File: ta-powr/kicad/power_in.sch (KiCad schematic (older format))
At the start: 29 parts, among them U1 SPV1040, U3 TLV8544DT, U4 ADS1115-Q1

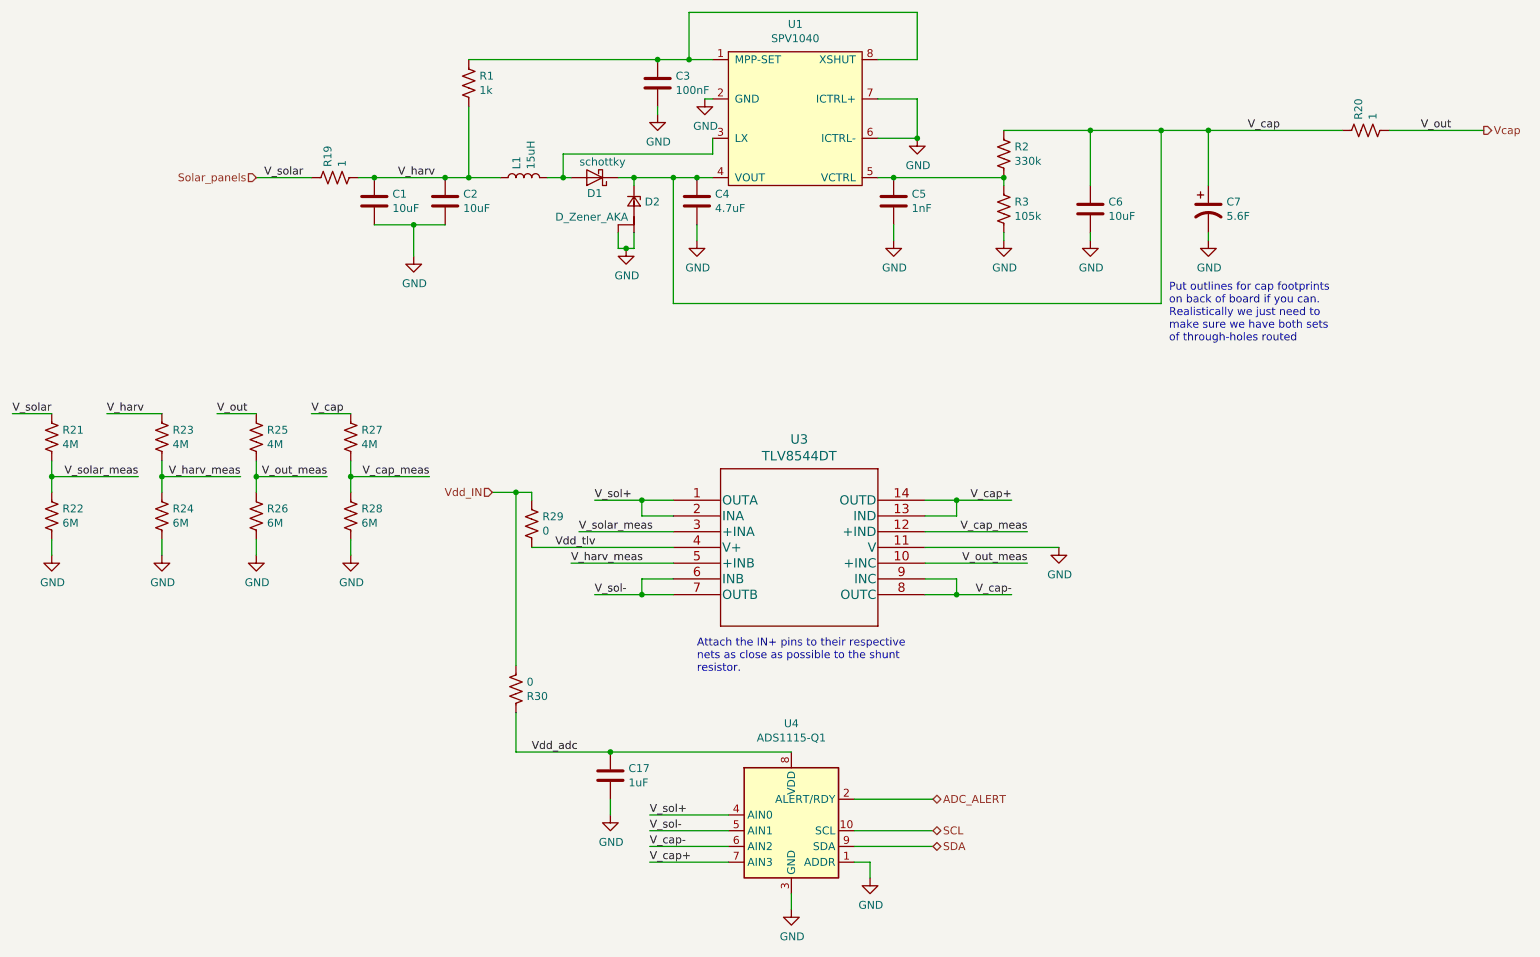
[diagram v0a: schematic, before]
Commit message: updated parts lists
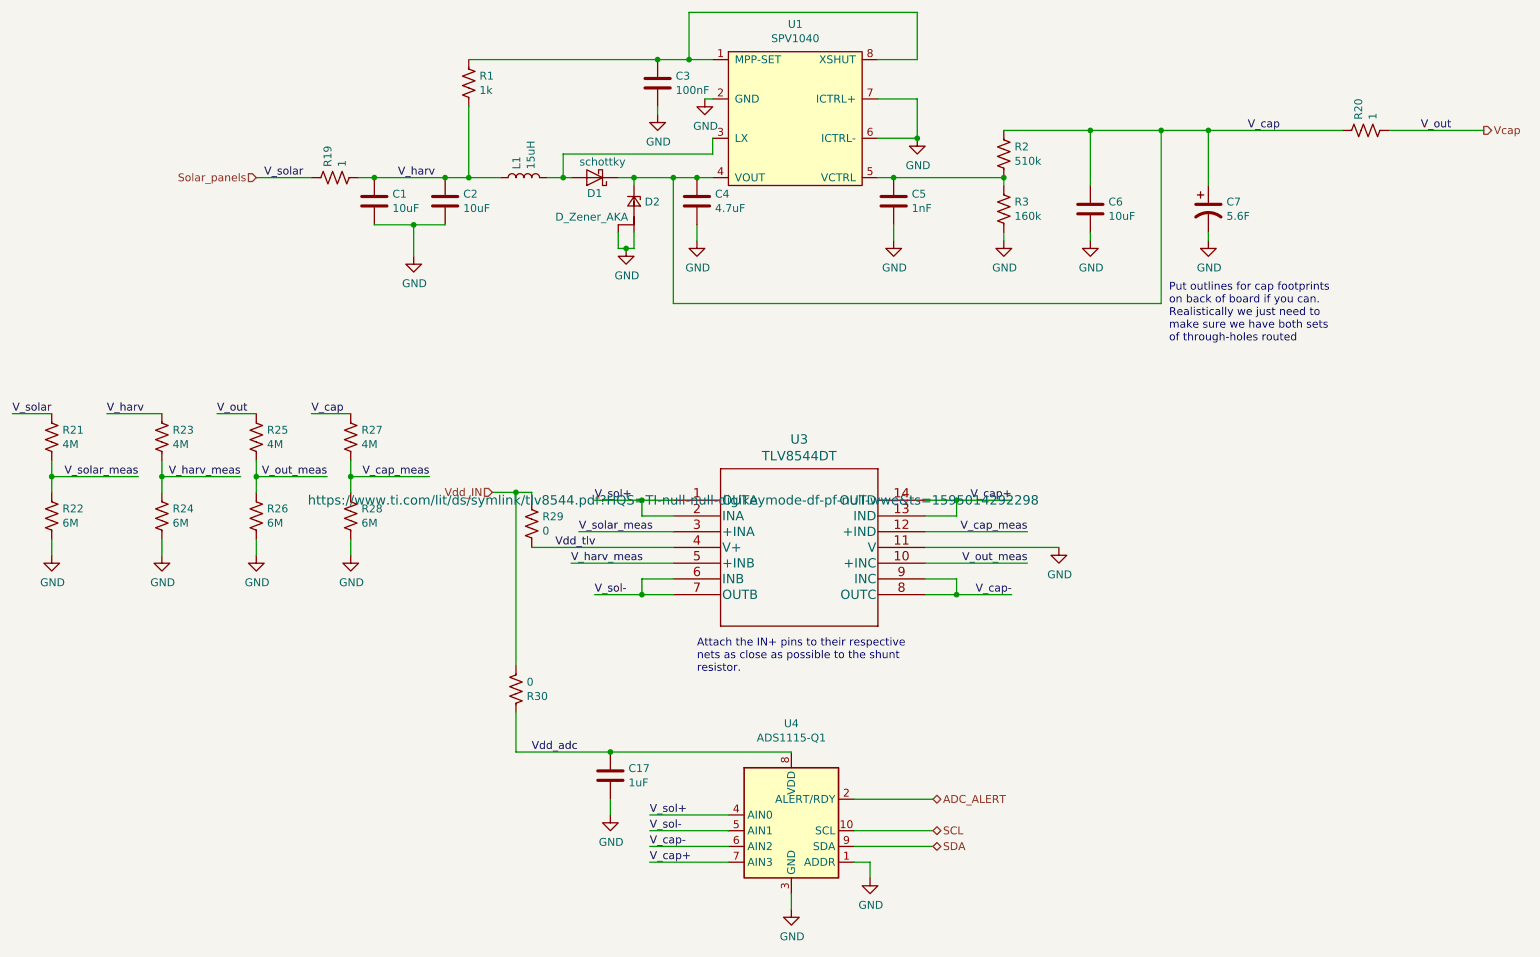
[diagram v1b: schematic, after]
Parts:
- C1, C2, C6: Manufacturer Part Number (none) -> C1608X7S0J106M080AC; Vendor (none) -> Digikey; Vendor Part Number (none) -> 445-9104-1-ND
- C17: Manufacturer Part Number (none) -> C0603C105K8RACTU; Vendor (none) -> Digikey; Vendor Part Number (none) -> 399-11133-1-ND
- C3: Manufacturer Part Number (none) -> C0603C104K8RACAUTO; Vendor (none) -> Digikey; Vendor Part Number (none) -> 399-17574-1-ND
- C4: Manufacturer Part Number (none) -> GCJ188C70J475KE02D; Vendor (none) -> Digikey; Vendor Part Number (none) -> 490-16480-1-ND
- C5: Manufacturer Part Number (none) -> C0603C102K8RACTU; Vendor (none) -> Digikey; Vendor Part Number (none) -> 399-8984-1-ND
- R1: Manufacturer Part Number (none) -> CRCW06031K00FKEAHP; Vendor (none) -> Digikey; Vendor Part Number (none) -> 541-1.00KSCT-ND
- R2: value 330k -> 510k; Manufacturer Part Number (none) -> ERJ-PA3F5103V; Vendor (none) -> Digikey; Vendor Part Number (none) -> P510KBYCT-ND
- R21, R23, R25, R27: Manufacturer Part Number (none) -> RMCF0603FT4M02; Vendor (none) -> Digikey; Vendor Part Number (none) -> RMCF0603FT4M02CT-ND
- R22, R24, R26, R28: Manufacturer Part Number (none) -> RMCF0603FT6M04; Vendor (none) -> Digikey; Vendor Part Number (none) -> RMCF0603FT6M04CT-ND
- R29, R30: Manufacturer Part Number (none) -> CRCW06030000Z0EAHP; Vendor (none) -> Digikey; Vendor Part Number (none) -> 541-0.0SBCT-ND
- R3: value 105k -> 160k; Manufacturer Part Number (none) -> ERJ-PA3F1603V; Vendor (none) -> Digikey; Vendor Part Number (none) -> P160KBYCT-ND
- U1: Manufacturer Part Number (none) -> SPV1040T; Vendor (none) -> Arrow; Vendor Part Number (none) -> SPV1040T
- U3: Manufacturer Part Number (none) -> TLV8544DT; Vendor (none) -> Digikey; Vendor Part Number (none) -> 296-49508-1-ND
- U4: Manufacturer Part Number (none) -> ADS1115BQDGSRQ1; Vendor (none) -> Digikey; Vendor Part Number (none) -> 296-45221-1-ND
